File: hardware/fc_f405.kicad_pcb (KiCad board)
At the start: 6 copper layers, 37 x 37 mm, 122 parts, among them J1 VBAT pads, J10 UART1 (RX), J11 UART2 (GPS), J12 UART3 (VTX), J13 UART5, J14 UART6, J15 CAM/RSSI/U4TX, J2 SWD pads, J3 BOOT pads, J4 I2C pads, J5 USB-C 16P, J6 JST-SH 8P, J7 Buzzer pads, J8 LED strip, J9 Video pads, Q1 CJAE10P06, Q2 2N7002, U1 STM32F405RGT7, U2 ICM-42688-P, U3 BMP388, U4 AT7456E, U5 W25Q128JVSIQ, U6 TPS54360DDAR, U7 TPS54360DDAR, U8 TLV1117-33IDCYR, U9 USBLC6-2SC6, Y1 8MHz, Y2 27MHz

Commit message: Update F405 flight controller: hardware revisions, production files, and ordering notes
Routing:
- net GND: track 108.7 -> 106.3 mm, vias 123 -> 120
- net +3V3_GYRO: track 26.5 -> 28.6 mm, vias 0 -> 2
- net GYRO_INT: track 10.3 -> 8.79 mm

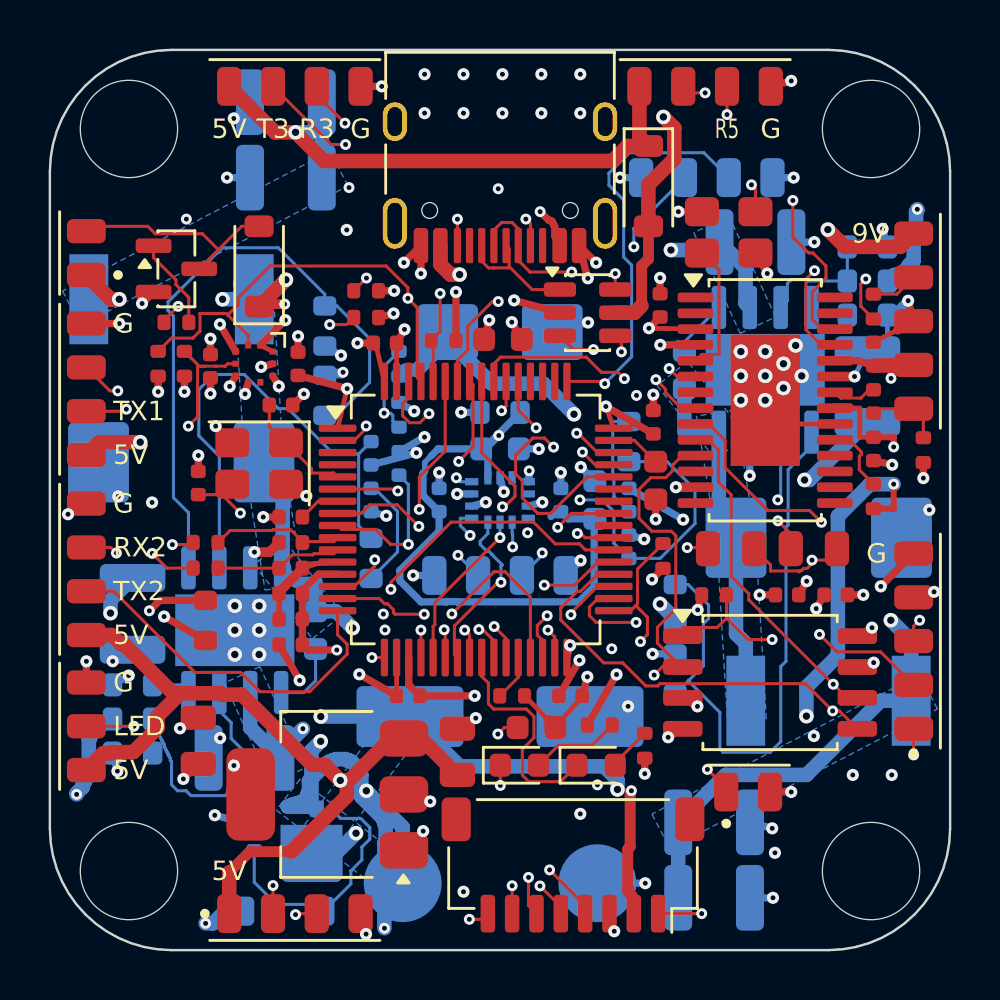
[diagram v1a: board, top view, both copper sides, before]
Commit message: Move vias off SMD pads for PCBWay DFM
PCBWay flagged vias in SMD pads (via-in-pad fill would cost over $100) and
a USB-C solder mask bridge below their 0.22 mm minimum.

- 31 fan-out vias that touched SMD pads are now off the pads: 20 moved on
  longer stubs, 6 GND vias replaced by pour stitching or dropped (pads sit
  on the GND pour), 5 hand-fixed in tight spots (U1.32, U4.23, U5.3, U6.7,
  U8 pin 2)
- Exposed-pad thermal vias under U4, U6 and U7 left as designed
- In3 RSSI_IN shifted 0.57 mm to make room for C41's ground via
- U8 (SOT-223) tab and pin 2 marked as one internal node
- DRC: 0 violations, 0 unconnected; production files regenerated
  (BOM, CPL and paste layers unchanged)
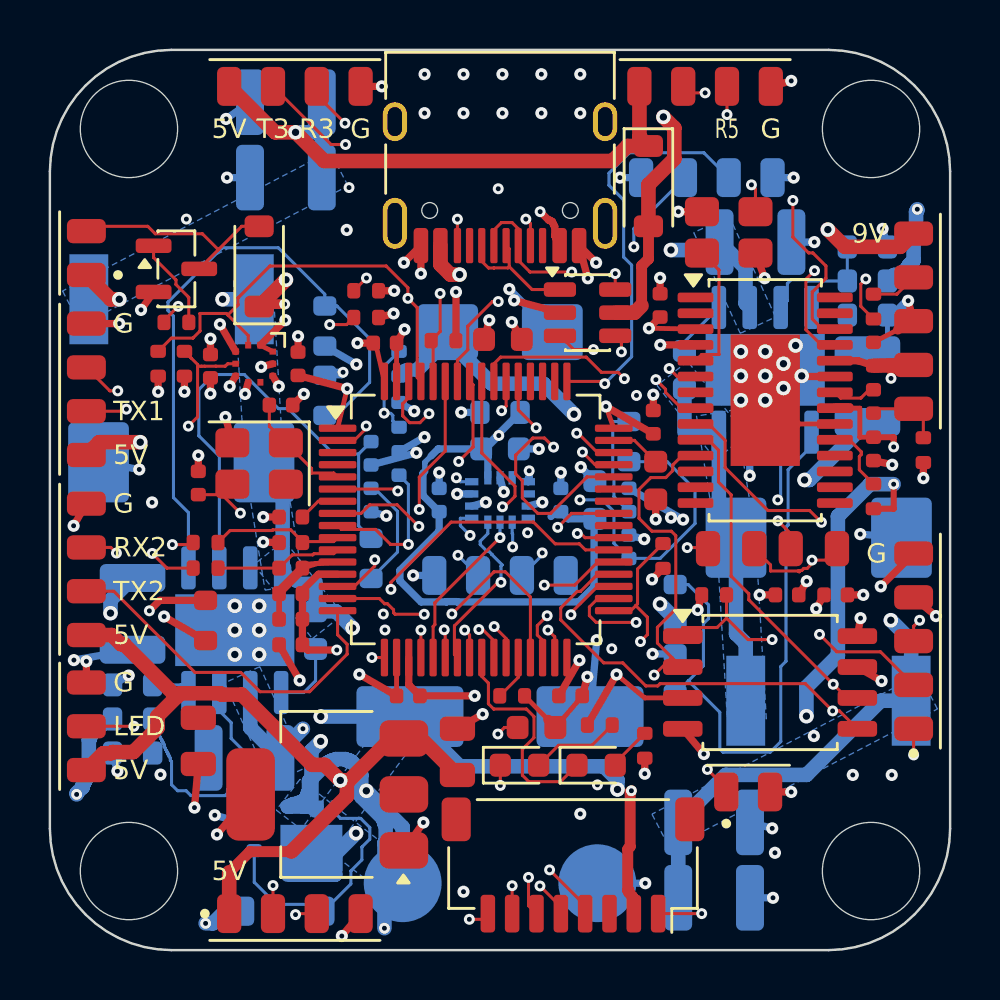
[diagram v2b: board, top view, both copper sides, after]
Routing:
- net +3V3: track 40.7 -> 44.0 mm, vias 31 -> 28
- net GND: track 106.3 -> 107.0 mm, vias 120 -> 115
